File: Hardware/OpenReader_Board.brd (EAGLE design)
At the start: 170.2 x 111.2 mm, 103 parts, among them IC1 BD5229G-TR, IC4 XC6220A331MR-G, J1 FH34SRJ-24S-0.5SH_99_, J2 SAMACSYS_PARTS_USB4110-GF-A, J3 QWIIC_RIGHT_ANGLE, J4 112A-TAAR-R03_ATTEND, Q1 20V/4.2A/52mΩ/1.4W, Q2 20V/4.2A/52mΩ/1.4W, Q3 SI1308EDL-T1-GE3, U1 W25Q512JVEIQ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

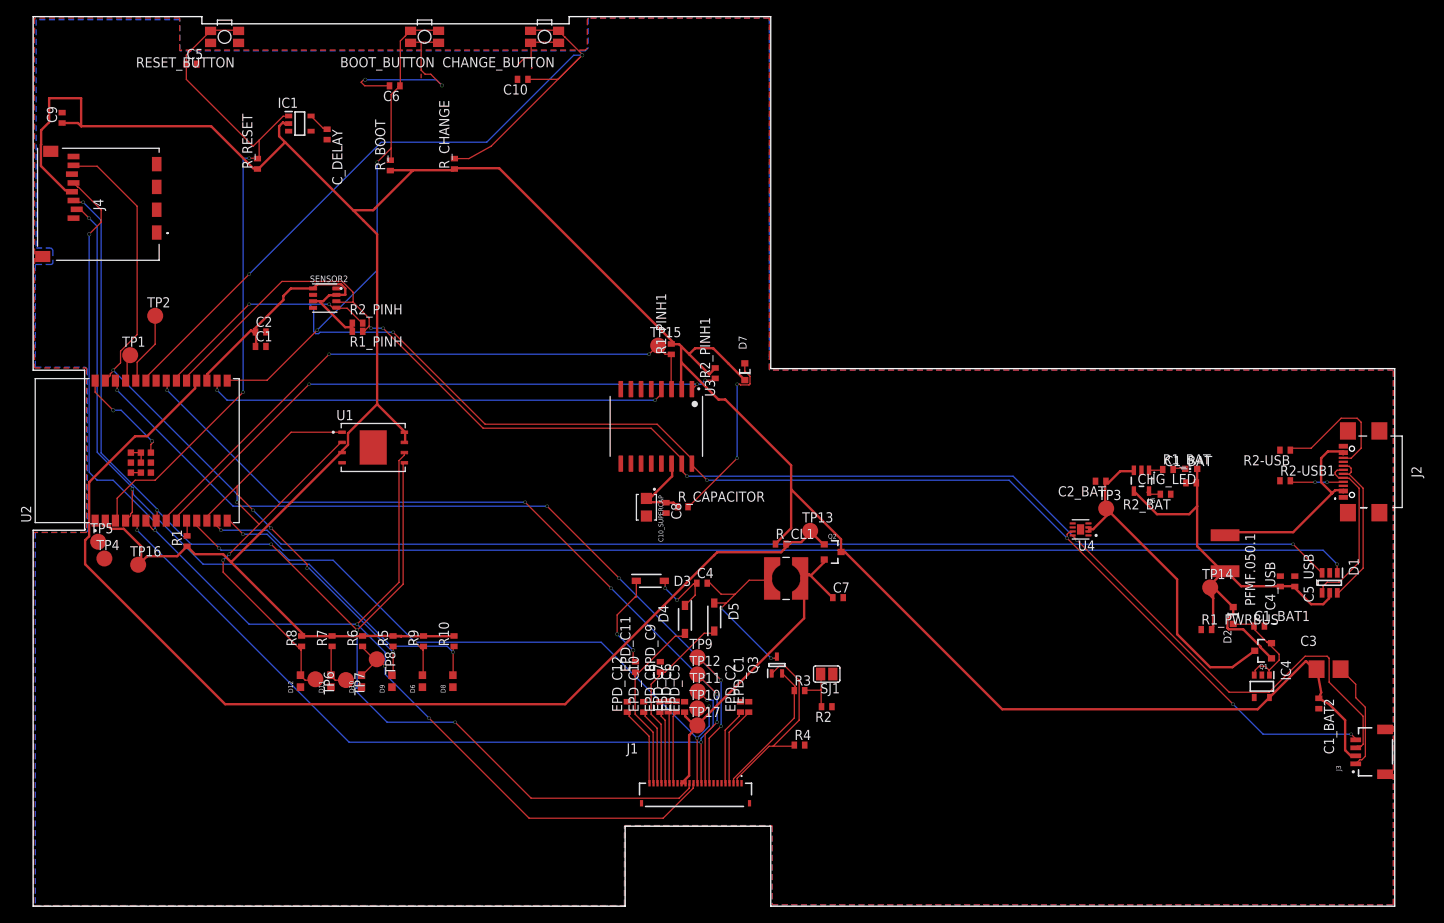
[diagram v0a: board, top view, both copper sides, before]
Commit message: Fixed reported issues and aditionally modified battery design and gerbers archive
- Fixed right angles
- Filled GND plane empty patches
- Created new and improved Display 3D design and battery 3D design
- Modified the board's dimensions
- Modified silkscreen to be more visible/readable
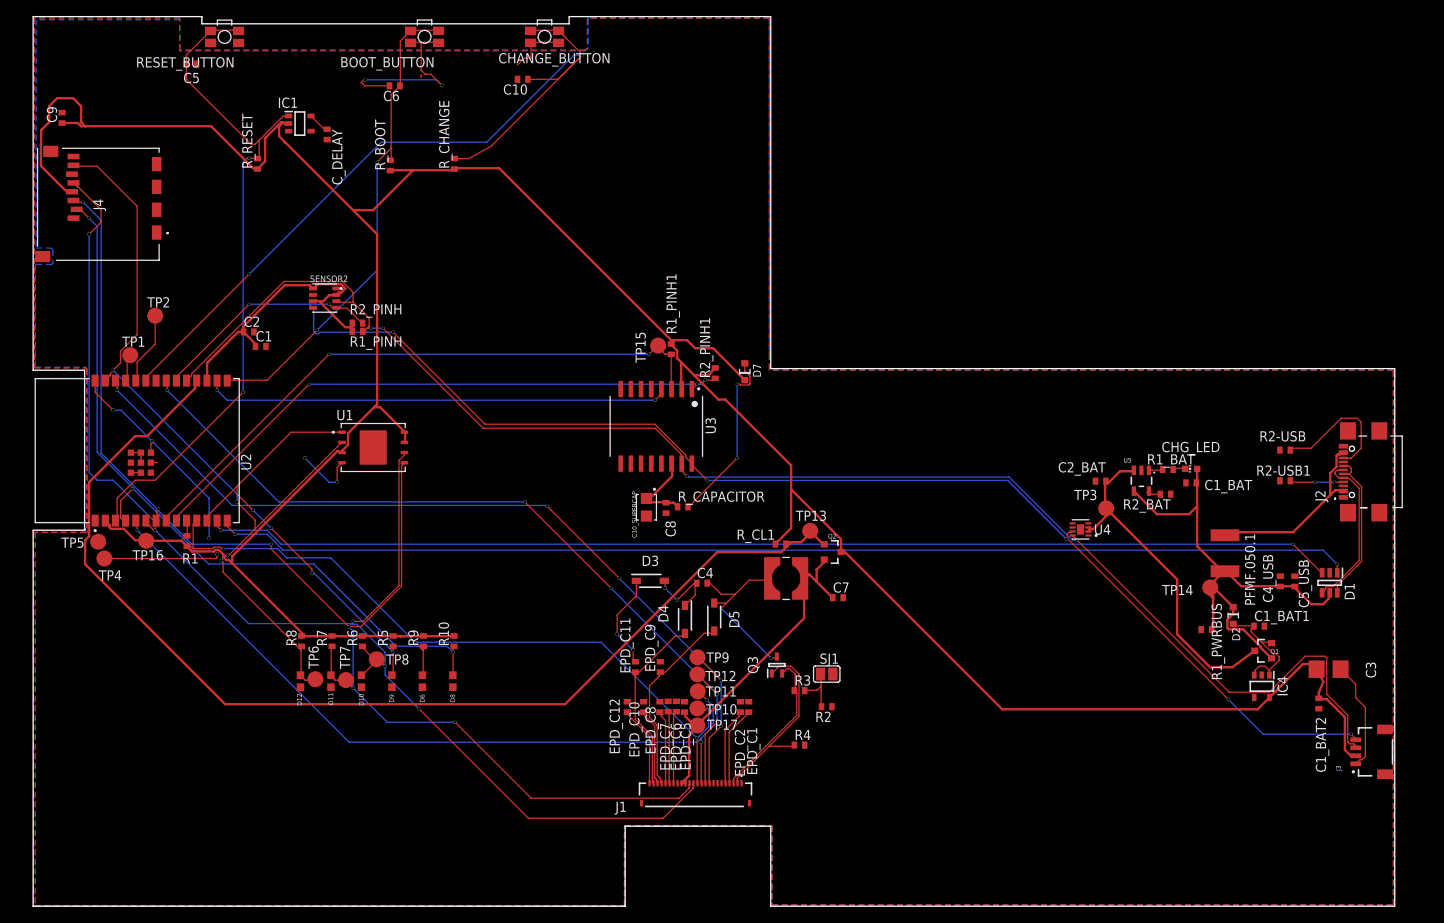
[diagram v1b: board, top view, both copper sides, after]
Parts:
- moved TP16 3.16 mm to (14.1, 45.7)
- moved C2 1.50 mm to (26.9, 71.8)
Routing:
- net GND: track 75.4 -> 113.7 mm, vias 6 -> 10
- net EPD_CS: track 91.3 -> 93.6 mm
- net VUSB: track 26.1 -> 24.4 mm
- net 3V3: track 383.8 -> 382.1 mm
- net RESE: track 17.6 -> 19.3 mm
- net N$3: track 14.3 -> 15.4 mm
- net SCK: track 168.7 -> 169.7 mm
- net MISO: track 102.4 -> 103.1 mm
- net GDR: track 23.6 -> 24.2 mm
- net RESET: track 86.4 -> 85.9 mm
